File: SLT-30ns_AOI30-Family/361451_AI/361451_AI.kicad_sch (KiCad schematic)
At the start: 9 parts, among them T1 IBM_Transistor, U1 12-Pin_SLx_Can

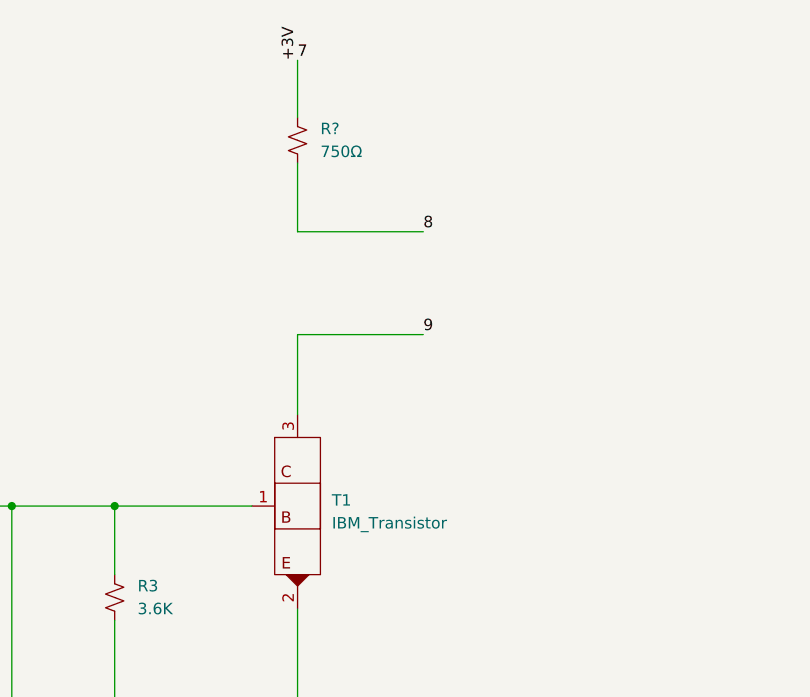
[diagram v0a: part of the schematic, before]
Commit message: Finished off the SLT-30 family of parts, started on the SLT-700 family. Changed labeling of transistors and diodes in all schematics, but have yet to update all the pdf files. This is a TODO...
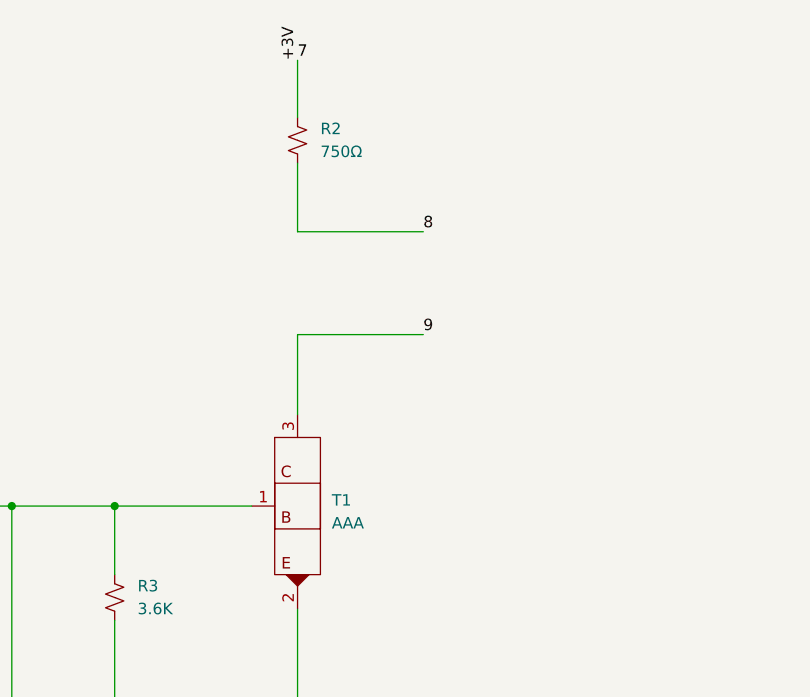
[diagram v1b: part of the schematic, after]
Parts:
- T1: value IBM_Transistor -> AAA
- gave numbers to parts that had none: 1
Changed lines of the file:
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@@
       (effects (font (size 1.27 1.27)) (justify left))
     )
-    (property "Value" "IBM_Transistor" (id 1) (at 153.67 95.8849 0)
+    (property "Value" "AAA" (id 1) (at 153.67 95.8849 0)
       (effects (font (size 1.27 1.27)) (justify left))
     )
@@
   (symbol (lib_id "Device:R_Small_US") (at 149.86 53.34 0) (unit 1)
     (in_bom yes) (on_board yes) (fields_autoplaced)
-    (property "Reference" "R?" (id 0) (at 152.4 52.0699 0)
+    (property "Reference" "R2" (id 0) (at 152.4 52.0699 0)
       (effects (font (size 1.27 1.27)) (justify left))
     )
@@
       (reference "R1") (unit 1) (value "2K") (footprint "Resistor_SMD:R_0201_0603Metric")
     )
+    (path "/94dd523f-5529-4374-bb00-a68226b4e5f7"
+      (reference "R2") (unit 1) (value "750Ω") (footprint "Resistor_SMD:R_0201_0603Metric")
+    )
     (path "/e3b34507-97c6-4732-8351-5f7d2bda9963"
       (reference "R3") (unit 1) (value "3.6K") (footprint "Resistor_SMD:R_0201_0603Metric")
     )
-    (path "/94dd523f-5529-4374-bb00-a68226b4e5f7"
-      (reference "R?") (unit 1) (value "750Ω") (footprint "Resistor_SMD:R_0201_0603Metric")
-    )
     (path "/5c986000-fc83-4495-a50f-9f4b94e485bc"
-      (reference "T1") (unit 1) (value "IBM_Transistor") (footprint "")
+      (reference "T1") (unit 1) (value "AAA") (footprint "")
     )
     (path "/75e072b9-86c1-407b-a1c4-16b7a7044004"

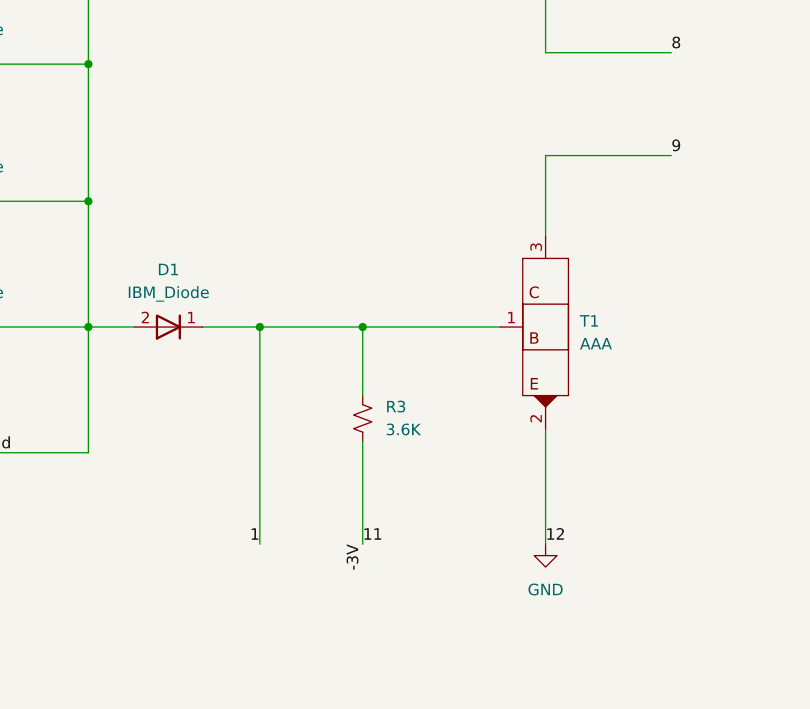
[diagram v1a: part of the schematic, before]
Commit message: Update schematic pdfs
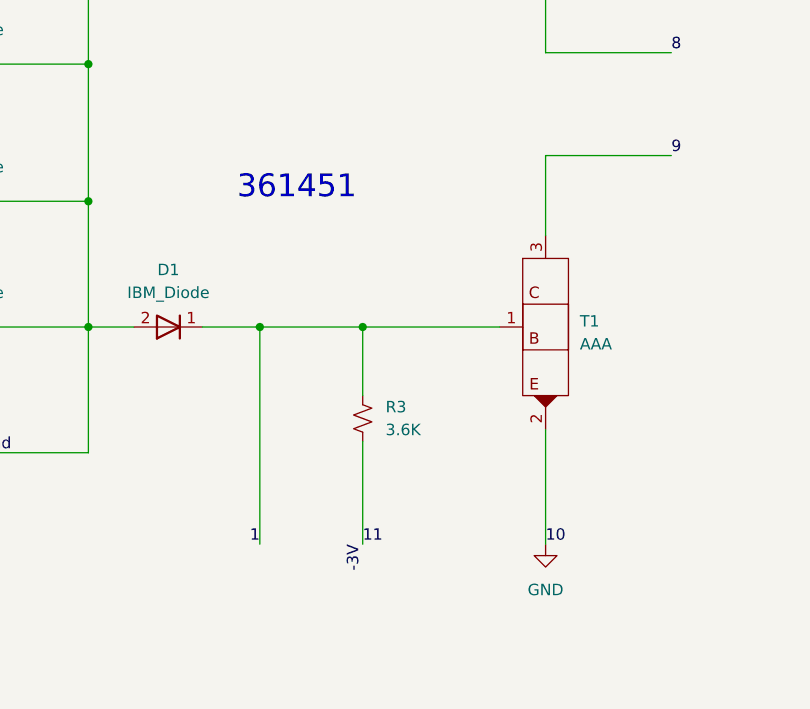
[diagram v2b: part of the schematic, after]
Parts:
- T1: footprint (none) -> Package_TO_SOT_SMD:SOT-883
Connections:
- net 10 is gone; now on net GND: U1.10
- net GND: no longer U1.12
- new net 12: U1.12
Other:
- note added: "361451"
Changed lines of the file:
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@@
     (stroke (width 0) (type default) (color 0 0 0 0))
   )
+  (text "361451" (at 115.57 80.01 0)
+    (effects (font (size 2.54 2.54)) (justify left bottom))
+  )
   (label "8" (at 163.83 63.5 0)
     (effects (font (size 1.27 1.27)) (justify left bottom))
@@
     (effects (font (size 1.27 1.27)) (justify left bottom))
   )
-  (label "12" (at 149.86 118.11 0)
-    (effects (font (size 1.27 1.27)) (justify left bottom))
-  )
   (label "2" (at 73.66 93.98 180)
     (effects (font (size 1.27 1.27)) (justify right bottom))
@@
   (label "1" (at 118.11 118.11 180)
     (effects (font (size 1.27 1.27)) (justify right bottom))
+  )
+  (label "10" (at 149.86 118.11 0)
+    (effects (font (size 1.27 1.27)) (justify left bottom))
   )
   (label "12" (at 234.95 144.78 270)
@@
       (effects (font (size 1.27 1.27)) (justify left))
     )
-    (property "Footprint" "" (id 2) (at 149.86 93.98 0)
+    (property "Footprint" "Package_TO_SOT_SMD:SOT-883" (id 2) (at 149.86 93.98 0)
       (effects (font (size 1.27 1.27)) hide)
     )
@@
     )
     (path "/5c986000-fc83-4495-a50f-9f4b94e485bc"
-      (reference "T1") (unit 1) (value "AAA") (footprint "")
+      (reference "T1") (unit 1) (value "AAA") (footprint "Package_TO_SOT_SMD:SOT-883")
     )
     (path "/75e072b9-86c1-407b-a1c4-16b7a7044004"
